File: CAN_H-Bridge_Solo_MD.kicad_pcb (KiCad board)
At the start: 2 copper layers, 84.3 x 36.3 mm, 49 parts, among them IC1 SI8650AB-B-IS1, IC2 A3921KLPTR-T, IC3 AP7381-50SA-7, J2 Conn_01x03, J3 Conn_01x05, J4 Bus_mechaken_PCIexpress_x16_1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, M1 Motor_DC, Q1 IRFB3806PBF, Q2 IRFB3806PBF, Q3 IRFB3806PBF, Q4 IRFB3806PBF, U1 LDL1117S33R_SOT223-4, U2 STM32F042K6Tx, U3 MCP2562-E-SN, U4 LDL1117S33TR_SOT223-4

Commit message: clean
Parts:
- J3: value Conn_01x05 -> Conthrough
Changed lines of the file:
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@@
   )
   (setup
-    (last_trace_width 0.4)
+    (last_trace_width 0.25)
     (user_trace_width 0.4)
     (user_trace_width 0.5)
@@
       (effects (font (size 1 1) (thickness 0.15)))
     )
-    (fp_text value Conn_01x05 (at 0 12.49 90) (layer F.Fab)
-      (effects (font (size 1 1) (thickness 0.15)))
+    (fp_text value Conthrough (at 2.1 5.1 180) (layer B.SilkS)
+      (effects (font (size 1 1) (thickness 0.15)) (justify mirror))
     )
     (fp_line (start -0.635 -1.27) (end 1.27 -1.27) (layer F.Fab) (width 0.1))
@@
   )
   (gr_line (start 156.15 116.75) (end 78.85 116.75) (layer Edge.Cuts) (width 0.1))
-  (gr_text GND (at 110 118.4) (layer F.SilkS)
-    (effects (font (size 0.6 0.6) (thickness 0.09)) (justify mirror))
-  )
-  (gr_text VCP_TX (at 107.6 117.6) (layer F.SilkS)
-    (effects (font (size 0.6 0.6) (thickness 0.09)) (justify mirror))
-  )
-  (gr_text VCP_RX (at 104.8 118.4) (layer F.SilkS)
-    (effects (font (size 0.6 0.6) (thickness 0.09)) (justify mirror))
+  (gr_text GND (at 110 118.5) (layer F.SilkS)
+    (effects (font (size 0.8 0.8) (thickness 0.12)) (justify mirror))
+  )
+  (gr_text VCP_TX (at 107.6 117.4) (layer F.SilkS)
+    (effects (font (size 0.8 0.8) (thickness 0.12)) (justify mirror))
+  )
+  (gr_text VCP_RX (at 104.8 118.5) (layer F.SilkS)
+    (effects (font (size 0.8 0.8) (thickness 0.12)) (justify mirror))
   )
   (gr_text NRST (at 100.2 118.4) (layer B.SilkS)
-    (effects (font (size 0.6 0.6) (thickness 0.09)) (justify mirror))
-  )
-  (gr_text SWDIO (at 97.6 118) (layer B.SilkS)
-    (effects (font (size 0.6 0.6) (thickness 0.09)) (justify mirror))
+    (effects (font (size 0.8 0.8) (thickness 0.12)) (justify mirror))
+  )
+  (gr_text SWDIO (at 97.6 117.4) (layer B.SilkS)
+    (effects (font (size 0.8 0.8) (thickness 0.12)) (justify mirror))
   )
   (gr_text GND (at 95.2 118.4) (layer B.SilkS)
-    (effects (font (size 0.6 0.6) (thickness 0.09)) (justify mirror))
-  )
-  (gr_text SWCLK (at 92.6 118) (layer B.SilkS)
-    (effects (font (size 0.6 0.6) (thickness 0.09)) (justify mirror))
+    (effects (font (size 0.8 0.8) (thickness 0.12)) (justify mirror))
+  )
+  (gr_text SWCLK (at 92.6 117.4) (layer B.SilkS)
+    (effects (font (size 0.8 0.8) (thickness 0.12)) (justify mirror))
   )
   (gr_text 3V3 (at 90 118.4) (layer B.SilkS)
-    (effects (font (size 0.6 0.6) (thickness 0.09)) (justify mirror))
+    (effects (font (size 0.8 0.8) (thickness 0.12)) (justify mirror))
   )
   (gr_line (start 159.65 120.25) (end 159.65 153.05) (layer Edge.Cuts) (width 0.1))

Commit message: fix
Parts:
- moved M1 1.00 mm to (146.0, 134.4)
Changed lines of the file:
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@@
   )
   (module XT60:XT60PW (layer B.Cu)
-    (at 145 134.4 90)
+    (at 146 134.4 90)
     (descr XT60)
     (tags Connector)

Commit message: change
反転前
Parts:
- removed the C14 at (96.7, 143.7)
- removed the C15 at (96.7, 149.3)
- removed the IC3 at (100.5, 145.8)
- C7: renamed from C13; value 4.7uF -> 1uF
- Q1, Q2, Q3, Q4: value IRFB3806PBF -> TK6R7P06PLRQ; footprint Package_TO_SOT_THT:TO-220-3_Vertical -> Package_TO_SOT_SMD:TO-252-2
- S1: value IKD0403101 -> DIPSW; footprint SamacSys_Parts:SOP254P980X370-8N -> Package_DIP:DIP-8_W7.62mm
- U3: renamed from U4; value LDL1117S33TR_SOT223-4 -> MCP1799T-3302H/TT; footprint Package_TO_SOT_SMD:SOT-223-3_TabPin2 -> Package_TO_SOT_SMD:SOT-23
- moved Q3 31.9 mm to (146.2, 123.8), turned to 180 degrees
- moved R12 30.8 mm to (113.7, 145.3)
- moved Q2 29.8 mm to (126.2, 145.1), turned to 180 degrees
- moved C6 7.15 mm to (98.2, 146.6), turned to 0 degrees
- moved C12 6.43 mm to (123.0, 131.0)
- moved R9 5.27 mm to (118.6, 129.2)
- moved S1 4.61 mm to (86.5, 123.0)
- moved Q1 2.90 mm to (126.3, 123.9), turned to 180 degrees
- moved U3 2.84 mm to (98.2, 142.2), turned to 180 degrees
- moved D2 2.70 mm to (79.6, 121.1)
- moved D3 2.70 mm to (79.6, 118.1)
- moved R2 2.70 mm to (84.2, 121.1)
- moved R3 2.70 mm to (84.2, 118.1)
- moved R10 2.61 mm to (124.0, 137.8)
- moved Q4 2.22 mm to (146.3, 145.2), turned to 180 degrees
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- renumbered C3 to C1, C7 to C10, C6 to C11, C8 to C12, C12 to C13, C9 to C14, C10 to C15, C1 to C2, C2 to C3, C11 to C6, C5 to C8, C4 to C9, D6 to D1, D1 to D2, D2 to D3, D3 to D4, D4 to D5, D5 to D6, IC1 to IC2, IC2 to IC3, J2 to J1, J3 to J2, J4 to J3, R5 to R1, R8 to R10, R4 to R11, R9 to R12, R1 to R2, R2 to R3, R10 to R4, R11 to R5, R12 to R6, R6 to R7, R7 to R8, R3 to R9, U3 to U4
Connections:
- net +3V3 renamed IC_3V3
- J3 pad B9: Net-(J4-PadB9) -> VCC
- Q2 pad 2: SA_0 -> VCC
- Q2 pad 3: GNDPWR -> SB_0
- Q3 pad 2: VCC -> SA_0
- Q3 pad 3: SB_0 -> GNDPWR
- R10 pad 1: Net-(Q3-Pad1) -> Net-(Q2-Pad1)
- R11 pad 2: Net-(Q2-Pad1) -> Net-(Q3-Pad1)
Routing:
- net Net-(Q4-Pad1): track 4.09 -> 38.1 mm
- net VCC: track 40.1 -> 72.1 mm, vias 8 -> 160
- net GLB_0: track 43.0 -> 11.8 mm
- net Net-(J4-PadB9): track 29.1 -> 0.00 mm
- net SB_0: track 27.9 -> 50.4 mm, vias 16 -> 57
- net GNDPWR: track 47.1 -> 62.6 mm
- net MD_3V3: track 33.5 -> 19.0 mm, vias 1 -> 0
- net SA_0: track 26.4 -> 39.0 mm, vias 15 -> 50
- net IC_3V3: track 75.6 -> 85.0 mm
- net /SWCLK: track 28.6 -> 37.6 mm
- net Net-(Q2-Pad1): track 4.24 -> 13.0 mm
- net Net-(Q1-Pad1): track 3.87 -> 12.5 mm
- net DIP_SW_2: track 10.6 -> 16.7 mm
- net VCP_RX: track 45.4 -> 51.1 mm
- net GHA_0: track 12.7 -> 7.25 mm
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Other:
- board size 84.3 x 36.3 mm -> 84.3 x 40.1 mm
- board text added: "CAN H-Bridge Solo MD Prototype 2.0"
- board text removed: "CAN H-Bridge Solo MD Prototype 1.2"

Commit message: change
FET反転
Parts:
- M1: moved to F.Cu
- Q1, Q2, Q3, Q4: moved to B.Cu
- U2: value STM32F042K6Tx -> STM32F303K8
- turned M1 to 270 degrees
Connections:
- M1 pad 1: SB_0 -> SA_0
- M1 pad 2: SA_0 -> SB_0
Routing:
- net Net-(Q1-Pad1): track 12.5 -> 17.2 mm, vias 0 -> 1
- net Net-(Q2-Pad1): track 13.0 -> 8.31 mm, vias 0 -> 1
- net Net-(Q4-Pad1): track 38.1 -> 42.5 mm, vias 0 -> 1
- net Net-(Q3-Pad1): track 10.9 -> 7.24 mm, vias 0 -> 1
- net SB_0: track 50.4 -> 52.5 mm
- net SA_0: vias 50 -> 52

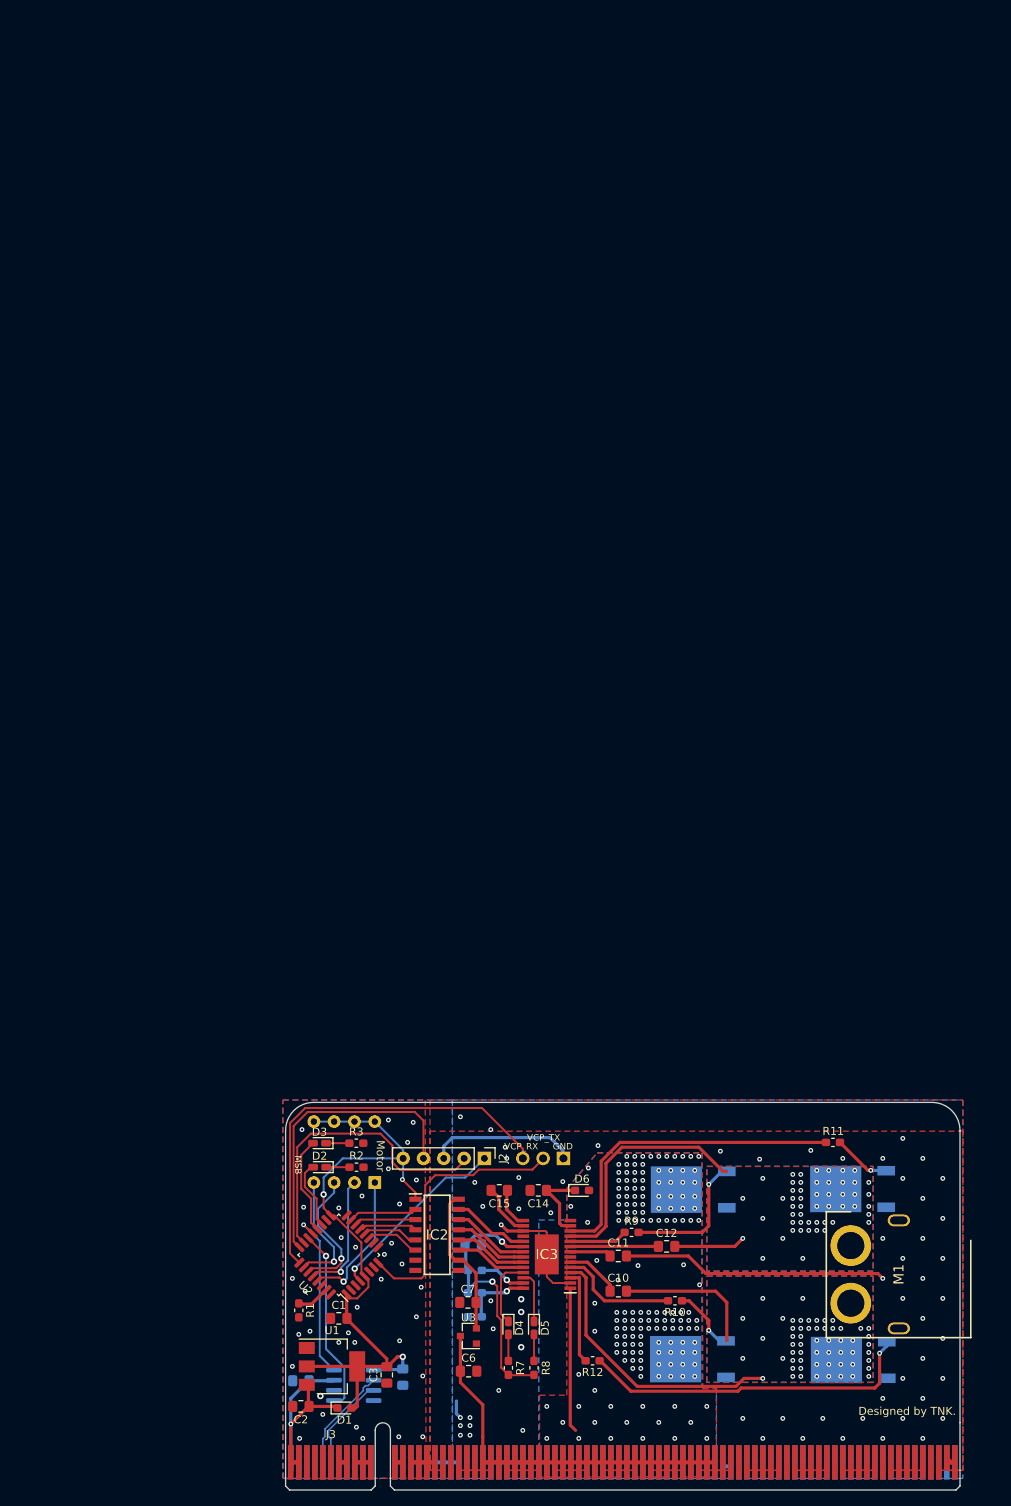
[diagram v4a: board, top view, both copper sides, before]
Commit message: change
モーターの許容電流を増加
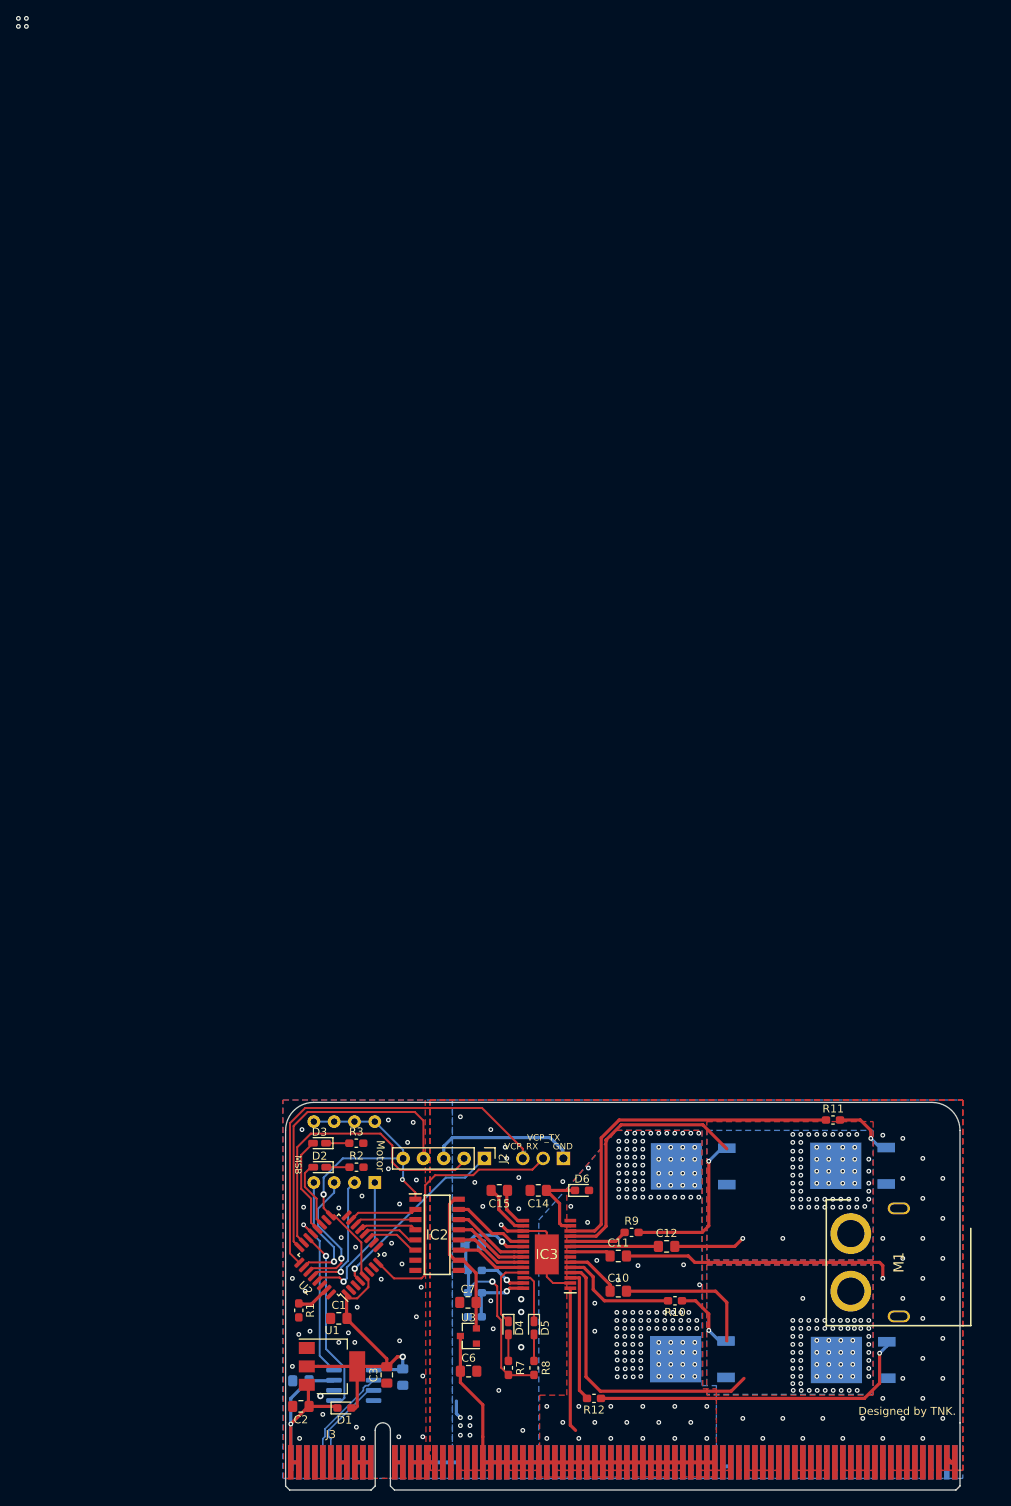
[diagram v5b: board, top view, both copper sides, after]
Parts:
- moved R12 4.70 mm to (113.9, 150.0)
- moved Q1 2.90 mm to (126.3, 121.0)
- moved Q3 2.90 mm to (146.2, 120.9)
- moved R11 2.80 mm to (143.8, 115.2)
- moved M1 1.50 mm to (146.0, 133.0)
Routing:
- net GLB_0: track 11.8 -> 16.5 mm
- net Net-(Q1-Pad1): track 17.2 -> 20.1 mm
- net GLA_0: track 41.2 -> 44.0 mm
- net SA_0: track 39.0 -> 41.8 mm, vias 52 -> 65
- net Net-(Q4-Pad1): track 42.5 -> 41.2 mm
- net SB_0: track 52.5 -> 53.7 mm, vias 57 -> 68
- net GNDPWR: track 62.6 -> 63.5 mm, vias 62 -> 56
- net Net-(Q3-Pad1): track 7.24 -> 7.79 mm
- net VCC: vias 160 -> 164
- net (no net): vias 0 -> 4

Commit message: change
ビアなどの増加
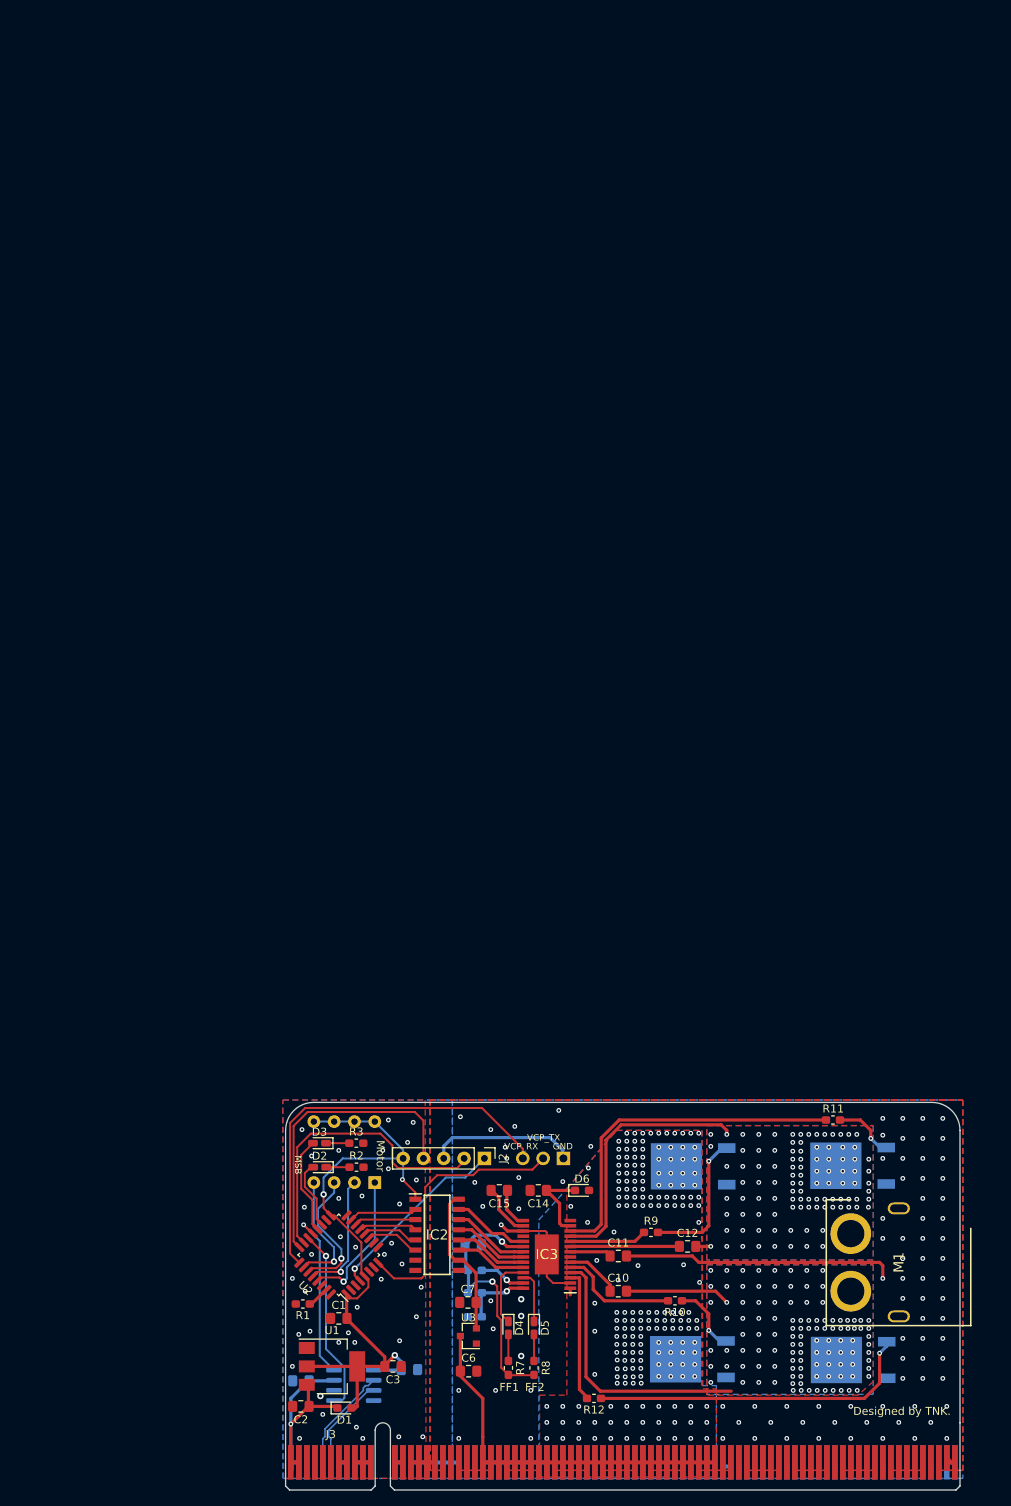
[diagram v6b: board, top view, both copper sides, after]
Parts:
- moved C12 2.62 mm to (125.6, 131.0)
- moved R9 2.43 mm to (121.0, 129.2)
- moved C3 1.32 mm to (88.8, 146.0), turned to 180 degrees
- moved C9 1.25 mm to (90.8, 146.4), turned to 180 degrees
- moved R1 0.94 mm to (77.5, 138.2), turned to 180 degrees
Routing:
- net VCC: track 72.1 -> 54.9 mm, vias 164 -> 197
- net SA_0: track 41.8 -> 34.3 mm, vias 65 -> 102
- net SB_0: track 53.7 -> 46.6 mm, vias 68 -> 112
- net Net-(C12-Pad1): track 11.0 -> 13.6 mm
- net Net-(Q1-Pad1): track 20.1 -> 17.7 mm
- net GHA_0: track 7.25 -> 9.68 mm
- net GNDPWR: track 63.5 -> 61.3 mm, vias 56 -> 92
- net /BOOT: track 4.20 -> 2.61 mm
- net IC_3V3: track 85.0 -> 84.2 mm
- net GND: vias 36 -> 39
- net (no net): vias 4 -> 0
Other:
- board text added: "FF1"
- board text added: "FF2"

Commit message: Release
Release Prototype-2.0
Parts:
- C3: value 4.7uF -> 2.2uF
- IC2: footprint SamacSys_Parts:SOIC127P600X175-16N -> Package_SO:SOIC-16_3.9x9.9mm_P1.27mm
- U1: value LDL1117S33R_SOT223-4 -> AP2210N-3.3TRG1; footprint Package_TO_SOT_SMD:SOT-223-3_TabPin2 -> Package_TO_SOT_SMD:SOT-23W_Handsoldering
- U3: footprint Package_TO_SOT_SMD:SOT-23 -> Package_TO_SOT_SMD:SOT-23_Handsoldering
- moved D1 9.31 mm to (78.9, 142.7)
- moved D5 8.38 mm to (104.0, 149.2), turned to 0 degrees
- moved R7 6.28 mm to (104.0, 139.9), turned to 180 degrees
- moved C3 2.91 mm to (85.9, 145.6)
- moved R8 2.46 mm to (104.0, 146.4), turned to 180 degrees
- moved C2 1.86 mm to (79.1, 151.0), turned to 0 degrees
- moved D4 1.73 mm to (103.9, 142.8), turned to 0 degrees
- moved U1 1.46 mm to (79.8, 146.6), turned to 180 degrees
- moved C6 1.00 mm to (97.2, 146.6)
- moved U3 0.50 mm to (97.7, 142.2)
- moved C1 0.30 mm to (82.0, 139.7)
- moved D3 0.20 mm to (79.6, 118.3)
- moved R3 0.15 mm to (84.2, 118.2)
- moved C7 0.06 mm to (98.2, 138.0)
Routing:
- net MD_FF2_0: track 6.56 -> 16.6 mm
- net IC_3V3: track 84.2 -> 80.3 mm
- net Net-(D5-Pad2): track 3.43 -> 6.60 mm
- net MD_FF1_0: track 8.96 -> 11.7 mm
- net V5: track 34.0 -> 31.6 mm
- net +5V: track 31.4 -> 32.5 mm
- net VCC: track 54.9 -> 55.7 mm, vias 197 -> 198
- net MD_3V3: track 19.0 -> 19.5 mm
- net GNDPWR: vias 92 -> 95
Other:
- board text added: "https://github.com/picopicodevil/CAN_H-Bridge_Solo_MD.git"
